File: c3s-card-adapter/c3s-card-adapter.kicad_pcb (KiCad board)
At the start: 4 copper layers, 19.4 x 34.6 mm, 2 parts, among them J1 SFM-120-02-L-DH, J2 SFM-120-02-L-DH

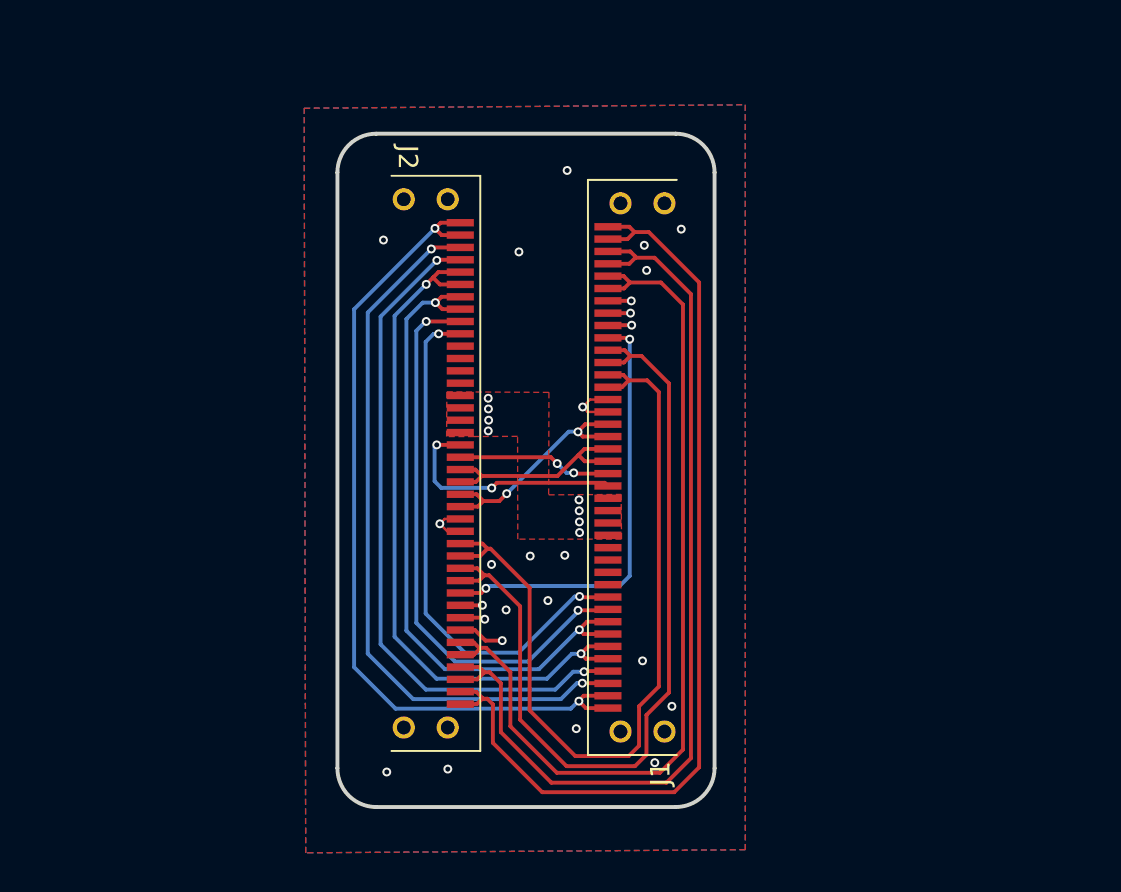
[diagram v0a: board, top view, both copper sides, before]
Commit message: Cleanup of v1.0 C3S card adapter. Should be good to go!
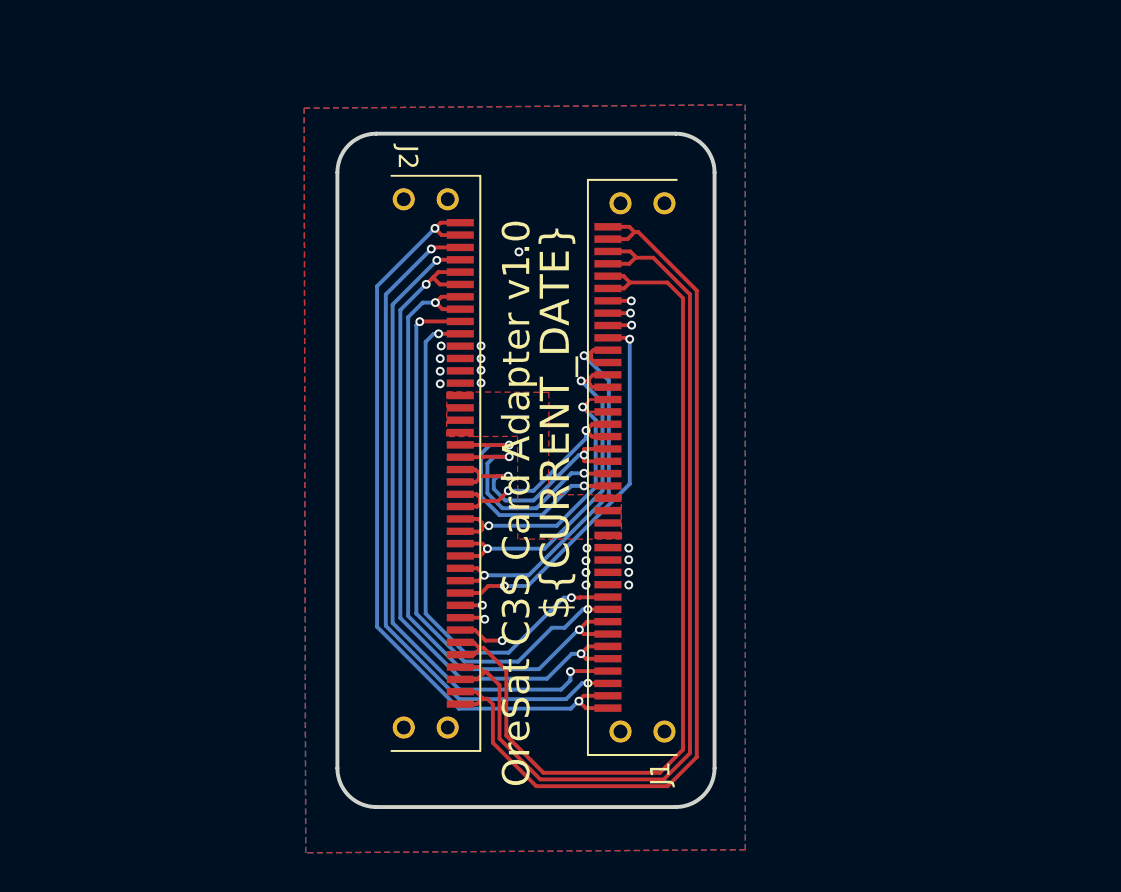
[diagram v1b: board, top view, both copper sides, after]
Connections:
- J1 pad 41: (no net) -> GND
- J1 pad 42: (no net) -> GND
- J1 pad 43: (no net) -> GND
- J1 pad 44: (no net) -> GND
- J2 pad 41: (no net) -> GND
- J2 pad 42: (no net) -> GND
- J2 pad 43: (no net) -> GND
- J2 pad 44: (no net) -> GND
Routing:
- net OPD_PWR: track 42.4 -> 16.6 mm
- net OPD_SCL: track 42.0 -> 19.1 mm, vias 0 -> 2
- net OPD_SDA: track 43.5 -> 21.1 mm, vias 0 -> 2
- net SPARE21: track 7.95 -> 12.6 mm
- net ~{SD}: track 43.0 -> 40.2 mm
- net CAN2_L: track 11.2 -> 14.1 mm, vias 0 -> 2
- net SPARE10: track 22.4 -> 19.6 mm
- net C3-UART-RX: track 37.4 -> 35.5 mm
- net SPARE22: track 12.4 -> 13.9 mm
- net SPARE09: track 24.2 -> 22.7 mm
- net C3-UART-TX: track 35.2 -> 34.0 mm
- net MAG-SDA: track 49.7 -> 48.7 mm
- net CAN1_L: track 36.4 -> 35.4 mm
- net CAN1_H: track 34.5 -> 33.9 mm
- net MAG-POWER: track 46.2 -> 46.7 mm
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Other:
- board text added: "OreSat C3S Card Adapter v${REVISION}"
- board text removed: "OreSat Flatsat Interface 1.0"

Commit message: Oh yeah stitching
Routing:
- net MAG-POWER: track 46.7 -> 42.1 mm
- net MAG-SCL: track 48.1 -> 44.7 mm
- net MAG-SDA: track 48.7 -> 47.0 mm
- net GND: vias 17 -> 41

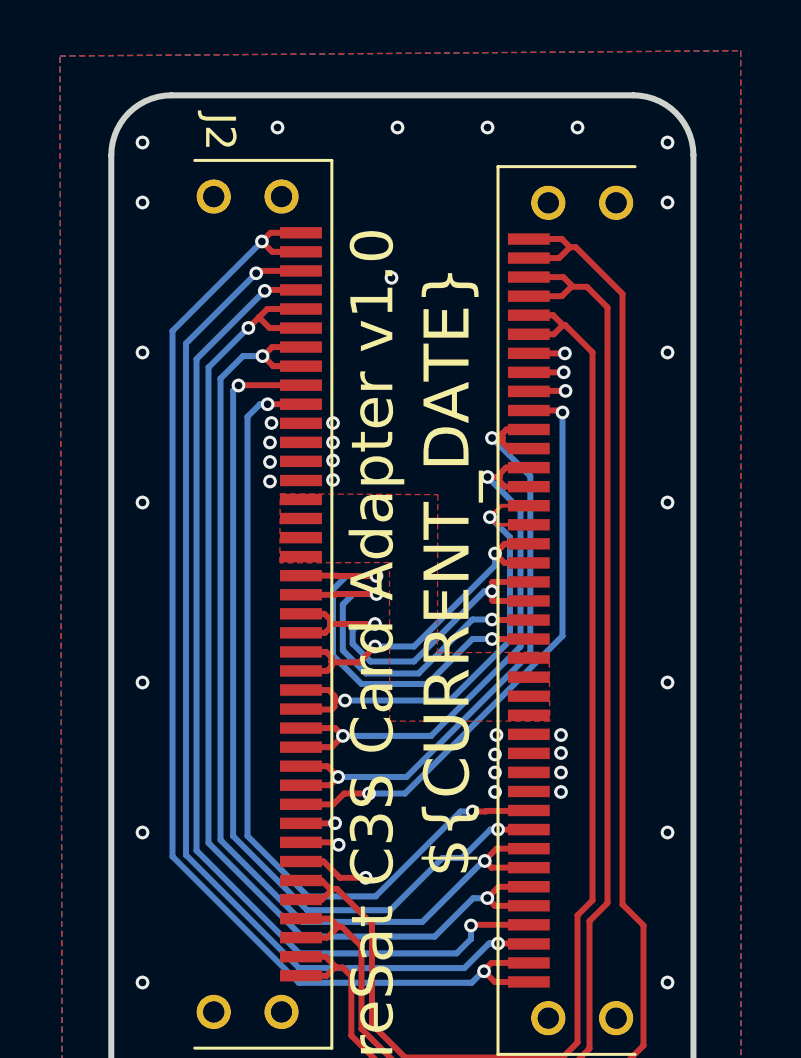
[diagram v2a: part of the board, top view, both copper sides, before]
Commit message: Sent v1.0 of the C3S adapter board off to fab!
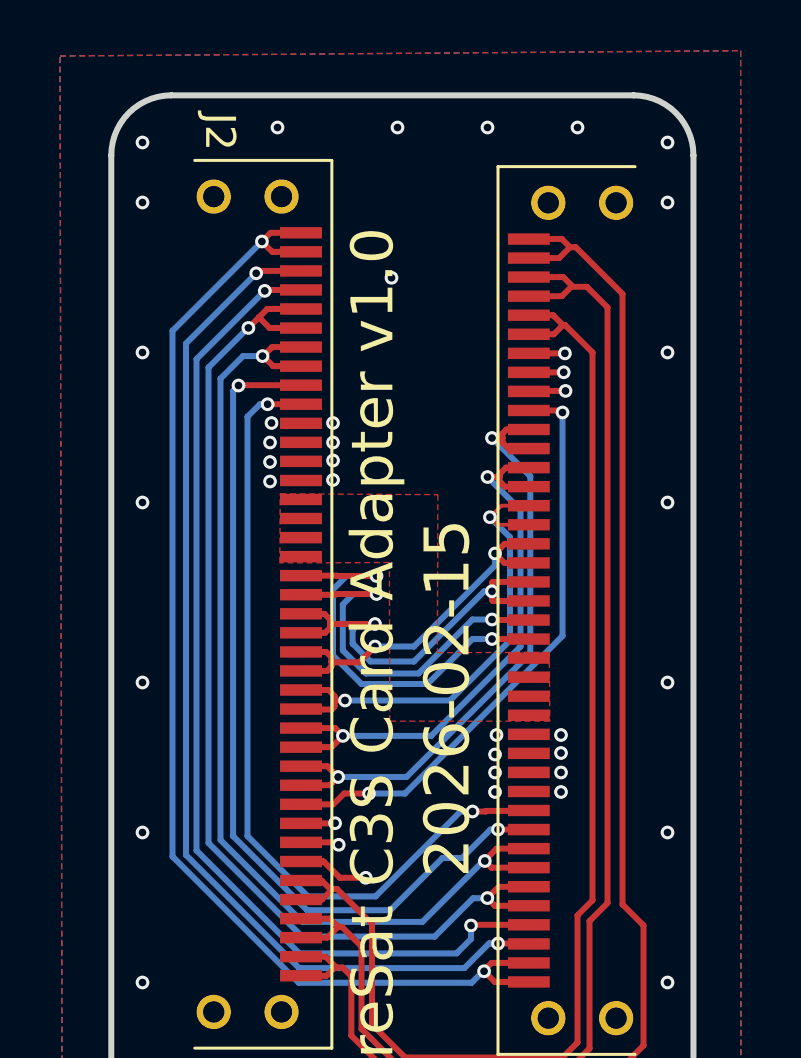
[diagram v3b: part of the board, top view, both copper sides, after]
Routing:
- removed copper zone on In2.Cu, net VBUS
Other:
- board text added: "${ISSUE_DATE}"
- board text removed: "${CURRENT_DATE}"
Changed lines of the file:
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@@
 		(layer "Edge.Cuts")
 	)
-	(gr_text "${CURRENT_DATE}"
+	(gr_text "${ISSUE_DATE}"
 		(at 155.55 94.5 90)
 		(layer "F.SilkS")
@@
 		(layer "B.Cu")
 		(net 23)
+	)
+	(zone
+		(net 2)
+		(net_name "VBUS")
+		(layer "F.Cu")
+		(hatch edge 0.5)
+		(priority 2)
+		(connect_pads
+			(clearance 0.127)
+		)
+		(min_thickness 0.25)
+		(filled_areas_thickness no)
+		(fill yes
+			(thermal_gap 0.5)
+			(thermal_bridge_width 0.5)
+			(smoothing fillet)
+			(radius 0.2)
+		)
+		(polygon
+			(pts
+				(xy 154.343438 81.738865) (xy 154.33 87.01) (xy 158.057908 86.989021) (xy 158.077076 89.289021)
+				(xy 152.74 89.289021) (xy 152.73 84) (xy 150.489584 84.01) (xy 149.077887 84.01) (xy 149.089743 81.71)
+			)
+		)
 	)
 	(zone
@@
 			)
 		)
-	)
-	(zone
-		(net 2)
-		(net_name "VBUS")
-		(layers "F.Cu" "In2.Cu")
-		(hatch edge 0.5)
-		(priority 2)
-		(connect_pads
-			(clearance 0.127)
-		)
-		(min_thickness 0.25)
-		(filled_areas_thickness no)
-		(fill yes
-			(thermal_gap 0.5)
-			(thermal_bridge_width 0.5)
-			(smoothing fillet)
-			(radius 0.2)
-		)
-		(polygon
-			(pts
-				(xy 154.343438 81.738865) (xy 154.33 87.01) (xy 158.057908 86.989021) (xy 158.077076 89.289021)
-				(xy 152.74 89.289021) (xy 152.73 84) (xy 150.489584 84.01) (xy 149.077887 84.01) (xy 149.089743 81.71)
-			)
-		)

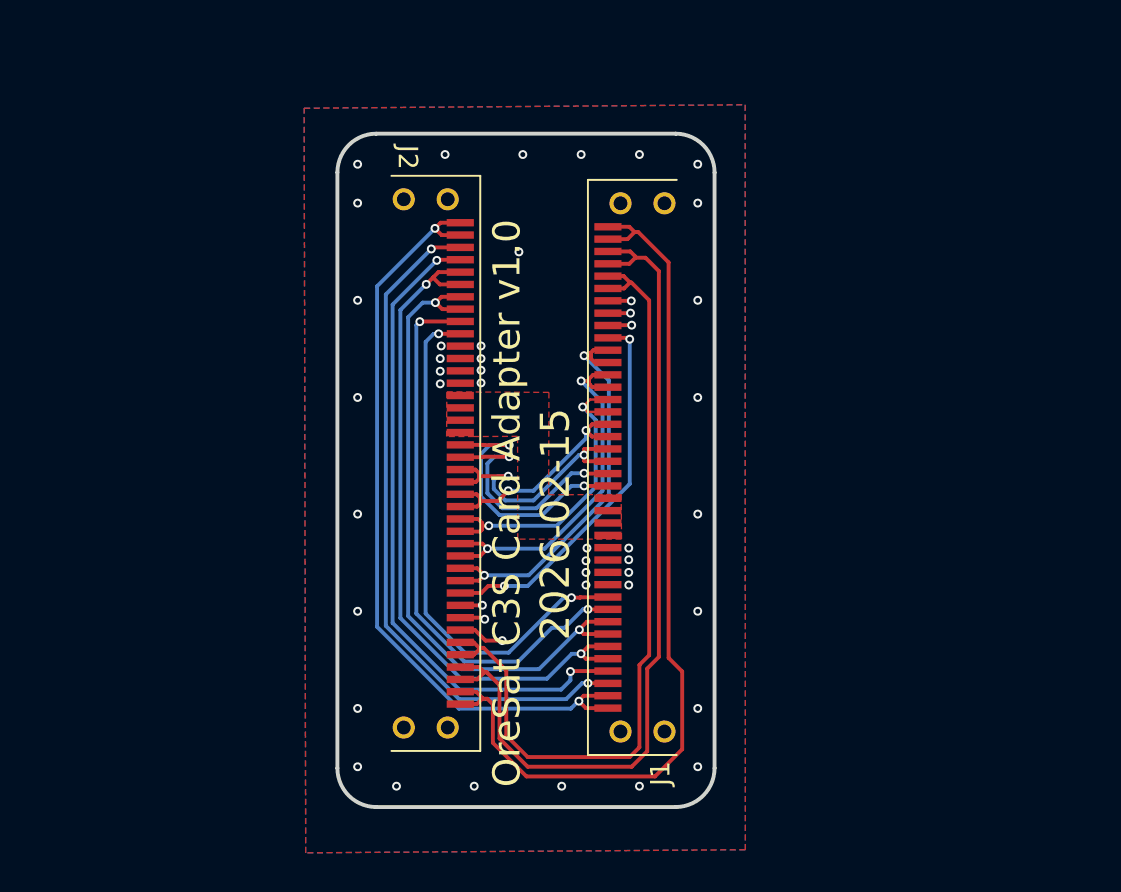
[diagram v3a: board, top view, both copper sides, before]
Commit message: C3S adapter board v1.1, now with generic pin-to-pin layout and a connector layout that doesn't crash the PCBs together.
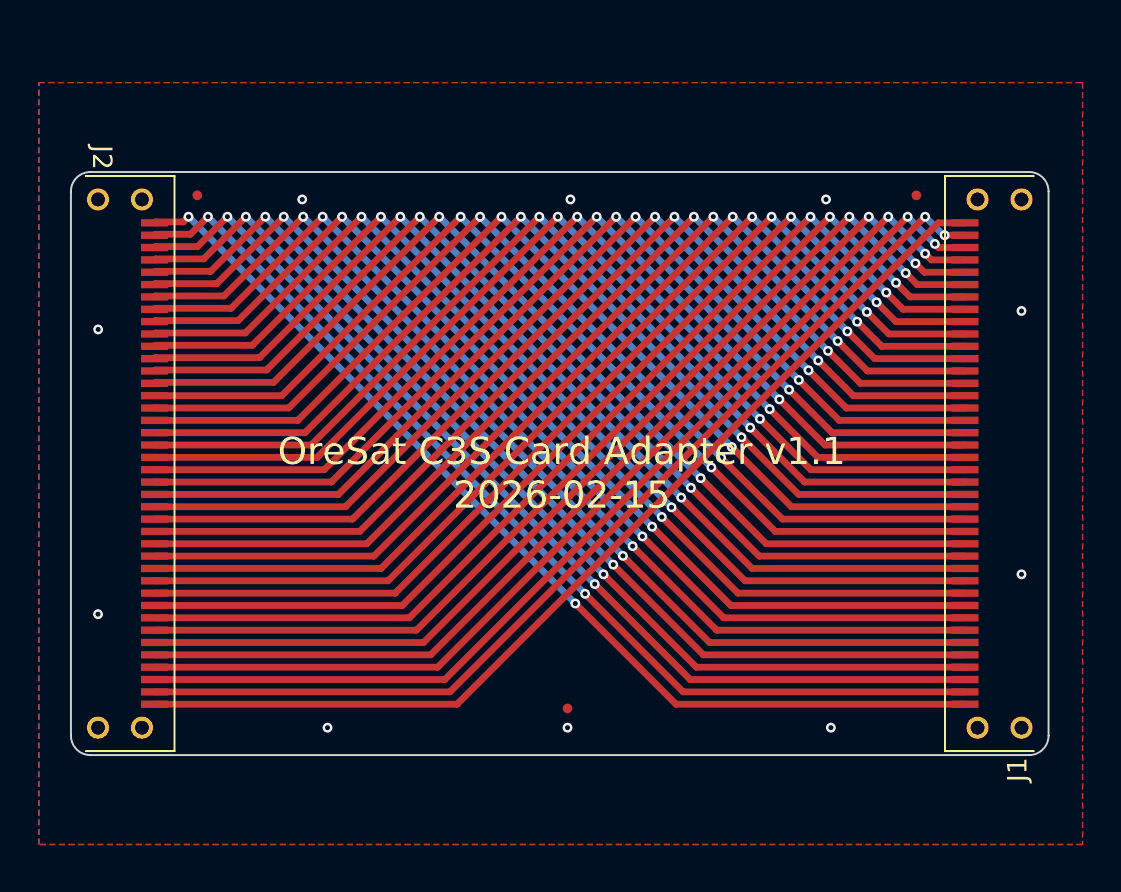
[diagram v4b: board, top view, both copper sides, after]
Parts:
- added FID1: Fiducial, Fiducial:Fiducial_0.5mm_Mask1mm, F.Cu at (136.2, 71.6)
- added FID2: Fiducial, Fiducial:Fiducial_0.5mm_Mask1mm, F.Cu at (155.3, 98.0)
- added FID3: Fiducial, Fiducial:Fiducial_0.5mm_Mask1mm, F.Cu at (173.2, 71.6)
- moved J1 18.4 mm to (179.8, 85.4)
- moved J2 15.7 mm to (130.0, 85.4)
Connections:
- net C3-UART-RX renamed Net-(J1-Pad38)
- net C3-UART-TX renamed Net-(J1-Pad37)
- net SPARE07 renamed Net-(J1-Pad7)
- net SPARE08 renamed Net-(J1-Pad8)
- net SPARE09 renamed Net-(J1-Pad9)
- net SPARE10 renamed Net-(J1-Pad10)
- net SPARE21 renamed Net-(J1-Pad21)
- net SPARE22 renamed Net-(J1-Pad22)
- net SPARE31 renamed Net-(J1-Pad31)
- net SPARE32 renamed Net-(J1-Pad32)
- J1 pad 1: MAG-SDA -> Net-(J1-Pad1)
- J1 pad 11: OPD_SDA -> Net-(J1-Pad11)
- J1 pad 12: OPD_SDA -> Net-(J1-Pad12)
- J1 pad 13: OPD_SCL -> Net-(J1-Pad13)
- J1 pad 14: OPD_SCL -> Net-(J1-Pad14)
- J1 pad 15: OPD_PWR -> Net-(J1-Pad15)
- J1 pad 16: OPD_PWR -> Net-(J1-Pad16)
- J1 pad 17: CAN2_H -> Net-(J1-Pad17)
- J1 pad 18: CAN2_H -> Net-(J1-Pad18)
- J1 pad 19: CAN2_L -> Net-(J1-Pad19)
- J1 pad 2: MAG-SDA -> Net-(J1-Pad2)
- J1 pad 20: CAN2_L -> Net-(J1-Pad20)
- J1 pad 23: VBUS -> Net-(J1-Pad23)
- J1 pad 24: VBUS -> Net-(J1-Pad24)
- J1 pad 25: VBUS -> Net-(J1-Pad25)
- J1 pad 26: VBUS -> Net-(J1-Pad26)
- J1 pad 27: GND -> Net-(J1-Pad27)
- J1 pad 28: GND -> Net-(J1-Pad28)
- J1 pad 29: GND -> Net-(J1-Pad29)
- J1 pad 3: MAG-SCL -> Net-(J1-Pad3)
- J1 pad 30: GND -> Net-(J1-Pad30)
- J1 pad 33: CAN1_H -> Net-(J1-Pad33)
- J1 pad 34: CAN1_H -> Net-(J1-Pad34)
- J1 pad 35: CAN1_L -> Net-(J1-Pad35)
- J1 pad 36: CAN1_L -> Net-(J1-Pad36)
- J1 pad 39: ~{SD} -> Net-(J1-Pad39)
- J1 pad 4: MAG-SCL -> Net-(J1-Pad4)
- J1 pad 40: ~{SD} -> Net-(J1-Pad40)
- J1 pad 5: MAG-POWER -> Net-(J1-Pad5)
- J1 pad 6: MAG-POWER -> Net-(J1-Pad6)
- J2 pad 1: MAG-SDA -> Net-(J1-Pad1)
- J2 pad 11: OPD_SDA -> Net-(J1-Pad11)
- J2 pad 12: OPD_SDA -> Net-(J1-Pad12)
- J2 pad 13: OPD_SCL -> Net-(J1-Pad13)
- J2 pad 14: OPD_SCL -> Net-(J1-Pad14)
- J2 pad 15: OPD_PWR -> Net-(J1-Pad15)
- J2 pad 16: OPD_PWR -> Net-(J1-Pad16)
- J2 pad 17: CAN2_H -> Net-(J1-Pad17)
- J2 pad 18: CAN2_H -> Net-(J1-Pad18)
- J2 pad 19: CAN2_L -> Net-(J1-Pad19)
- J2 pad 2: MAG-SDA -> Net-(J1-Pad2)
- J2 pad 20: CAN2_L -> Net-(J1-Pad20)
- J2 pad 23: VBUS -> Net-(J1-Pad23)
- J2 pad 24: VBUS -> Net-(J1-Pad24)
- J2 pad 25: VBUS -> Net-(J1-Pad25)
- J2 pad 26: VBUS -> Net-(J1-Pad26)
- J2 pad 27: GND -> Net-(J1-Pad27)
- J2 pad 28: GND -> Net-(J1-Pad28)
- J2 pad 29: GND -> Net-(J1-Pad29)
- J2 pad 3: MAG-SCL -> Net-(J1-Pad3)
- J2 pad 30: GND -> Net-(J1-Pad30)
- J2 pad 33: CAN1_H -> Net-(J1-Pad33)
- J2 pad 34: CAN1_H -> Net-(J1-Pad34)
- J2 pad 35: CAN1_L -> Net-(J1-Pad35)
- J2 pad 36: CAN1_L -> Net-(J1-Pad36)
- J2 pad 39: ~{SD} -> Net-(J1-Pad39)
- J2 pad 4: MAG-SCL -> Net-(J1-Pad4)
- J2 pad 40: ~{SD} -> Net-(J1-Pad40)
- J2 pad 5: MAG-POWER -> Net-(J1-Pad5)
- J2 pad 6: MAG-POWER -> Net-(J1-Pad6)
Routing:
- net Net-(J1-Pad3): track 0.00 -> 52.3 mm, vias 0 -> 2
- net Net-(J1-Pad2): track 0.00 -> 52.3 mm, vias 0 -> 2
- net Net-(J1-Pad33): track 0.00 -> 52.2 mm, vias 0 -> 2
- net Net-(J1-Pad19): track 0.00 -> 52.2 mm, vias 0 -> 2
- net Net-(J1-Pad6): track 0.00 -> 52.2 mm, vias 0 -> 2
- net Net-(J1-Pad5): track 0.00 -> 52.2 mm, vias 0 -> 2
- net Net-(J1-Pad30): track 0.00 -> 52.2 mm, vias 0 -> 2
- net Net-(J1-Pad25): track 0.00 -> 52.2 mm, vias 0 -> 2
- net Net-(J1-Pad24): track 0.00 -> 52.2 mm, vias 0 -> 2
- net Net-(J1-Pad11): track 0.00 -> 52.2 mm, vias 0 -> 2
- net Net-(J1-Pad40): track 0.00 -> 52.2 mm, vias 0 -> 2
- net Net-(J1-Pad39): track 0.00 -> 52.2 mm, vias 0 -> 2
- net Net-(J1-Pad36): track 0.00 -> 52.2 mm, vias 0 -> 2
- net Net-(J1-Pad35): track 0.00 -> 52.2 mm, vias 0 -> 2
- net Net-(J1-Pad34): track 0.00 -> 52.2 mm, vias 0 -> 2
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- removed copper zone on In1.Cu, net GND
- removed copper zone on In2.Cu, net GND
- removed copper zone on F.Cu, net VBUS
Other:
- board size 19.4 x 34.6 mm -> 50.3 x 30 mm
- copper layers 4 -> 2
- board text added: "OreSat C3S Card Adapter v${REVISION} ${ISSUE_DATE}"
- board text removed: "${ISSUE_DATE}"
- board text removed: "OreSat C3S Card Adapter v${REVISION}"
